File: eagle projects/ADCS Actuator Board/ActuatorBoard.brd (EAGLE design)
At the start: 91 x 91 mm, 232 parts, among them J11 TE_1-84953-1, J2 TE_1-84953-1, J4 TE_1-84953-1, J5 TE-1734829-3, U1 SIP2100DY-T1-GE3, U10 LM2917MX/NOPB, U12 TSV991AILT, U13 LM2917MX/NOPB, U14 ADS7841E_2K5, U16 DRV10970_MOTOR_DRIVERDRV10970, U17 LM2917MX/NOPB, U19 TSV991AILT, U2 SIP2100DY-T1-GE3, U20 ADS7841E_2K5, U3 SIP2100DY-T1-GE3, U6 DRV10970_MOTOR_DRIVERDRV10970, U7 DRV10970_MOTOR_DRIVERDRV10970, U8 TSV991AILT, U9 ADS7841E_2K5

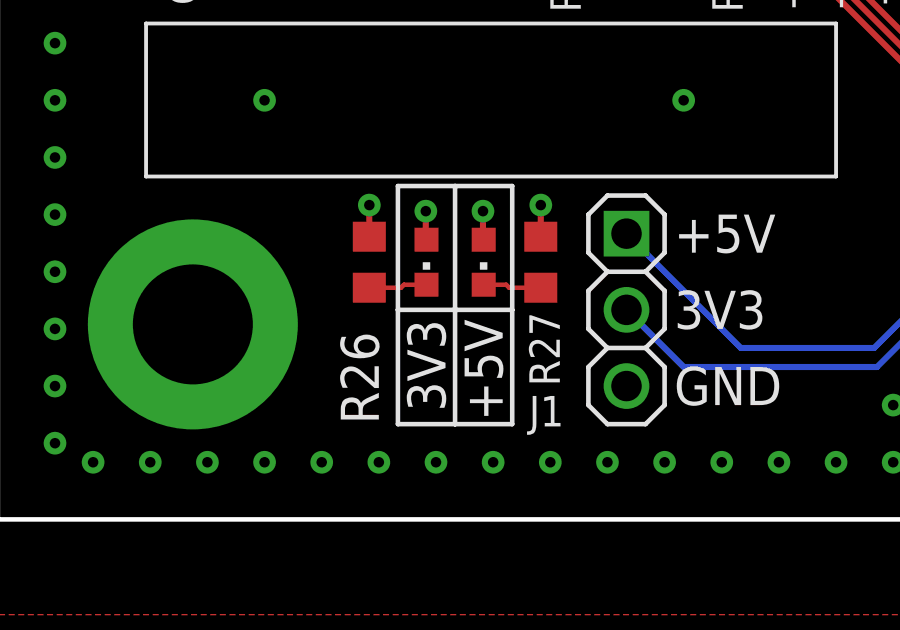
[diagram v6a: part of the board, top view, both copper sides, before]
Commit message: Removed LEDs from actuator board
Removed power reader LEDs from actuator boards.  Associated resistors were also removed and BOM was updated.
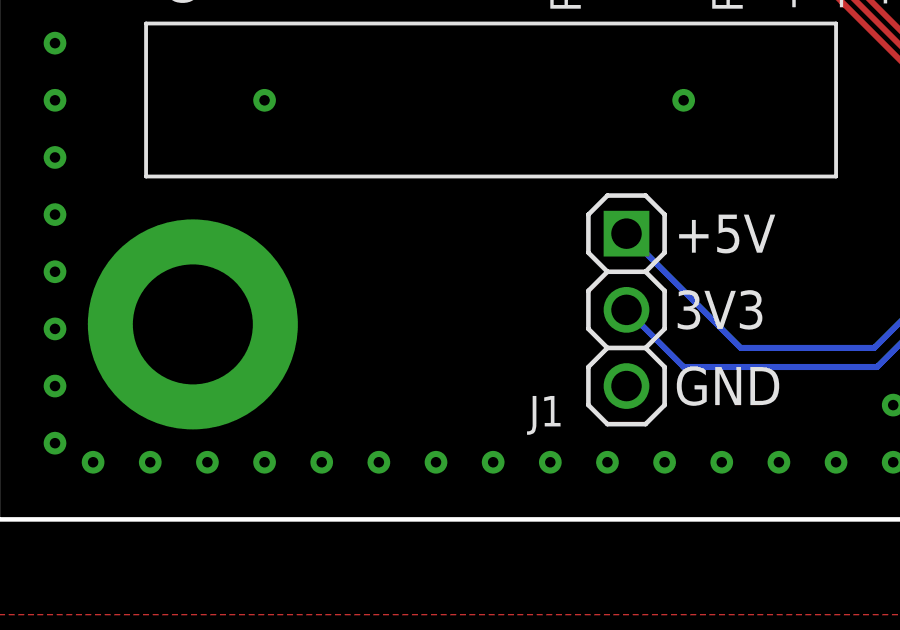
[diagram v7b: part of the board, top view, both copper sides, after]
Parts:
- removed LED1, LED2: (no value), led:CHIPLED_0603
- removed R26, R27: 470R, rcl:R0603
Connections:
- removed net N$14: LED2.C, R27.2
- removed net N$5: LED1.C, R26.2
- net +3V3: no longer LED2.A
- net +5V: no longer LED1.A
- net GND: no longer R26.1, R27.1
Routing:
- net GND: track 123.0 -> 120.9 mm, vias 358 -> 356
- net N$14: track 1.95 -> 0.00 mm
- net N$5: track 1.95 -> 0.00 mm
- net +3V3: track 77.8 -> 76.8 mm, vias 25 -> 24
- net +5V: track 108.0 -> 107.1 mm, vias 28 -> 27
